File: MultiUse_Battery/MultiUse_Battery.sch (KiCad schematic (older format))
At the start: 14 parts, among them IC1 ATMEGA328P-AU, P1 CONN_01X02, P2 CONN_01X01, P3 CONN_01X03, P4 CONN_01X03, P5 CONN_02X03, P6 CONN_01X02, P7 CONN_01X02, U1 MAX1724, U3 RFM69HW

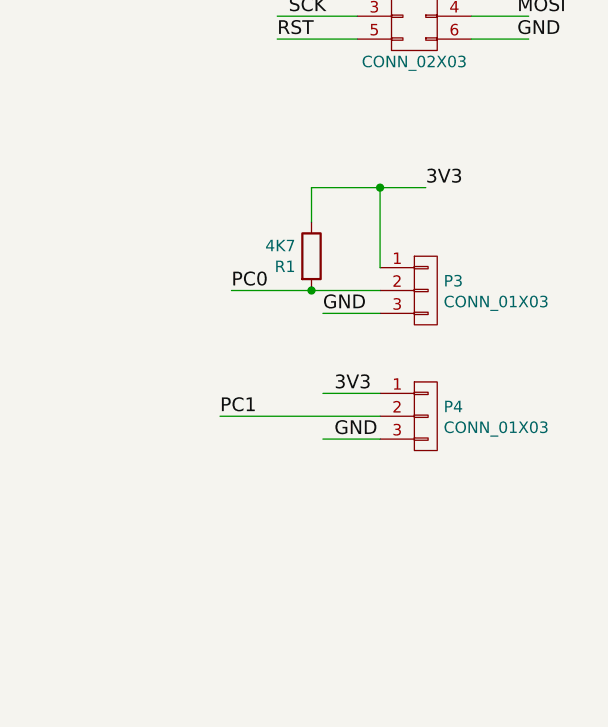
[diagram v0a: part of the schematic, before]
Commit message: Ajout README.md Modification orientation support pile CR2032 Ajout d'une PULLUP sur 2eme entrée
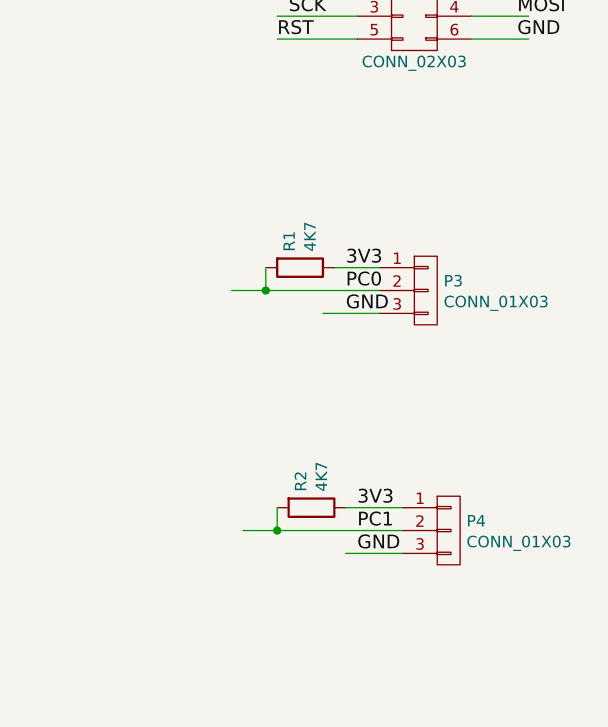
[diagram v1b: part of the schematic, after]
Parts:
- added R2: 4K7, Resistors_SMD:R_1206_HandSoldering, symbol R
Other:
- moved on the sheet: P4, R1
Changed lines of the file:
@@
 L CONN_01X03 P4
 U 1 1 587A3CDC
-P 9050 4400
-F 0 "P4" H 9128 4441 50  0000 L CNN
-F 1 "CONN_01X03" H 9128 4350 50  0000 L CNN
-F 2 "Pin_Headers:Pin_Header_Straight_1x03" H 9050 4400 50  0001 C CNN
-F 3 "" H 9050 4400 50  0000 C CNN
-	1    9050 4400
+P 9150 4900
+F 0 "P4" H 9228 4941 50  0000 L CNN
+F 1 "CONN_01X03" H 9228 4850 50  0000 L CNN
+F 2 "Pin_Headers:Pin_Header_Straight_1x03" H 9150 4900 50  0001 C CNN
+F 3 "" H 9150 4900 50  0000 C CNN
+	1    9150 4900
 	1    0    0    -1
 $EndComp
@@
 L R R1
 U 1 1 587A3DC5
-P 8550 3700
-F 0 "R1" H 8480 3654 50  0000 R CNN
-F 1 "4K7" H 8480 3745 50  0000 R CNN
-F 2 "Resistors_SMD:R_1206_HandSoldering" V 8480 3700 50  0001 C CNN
-F 3 "" H 8550 3700 50  0000 C CNN
-	1    8550 3700
-	1    0    0    -1
+P 8500 3750
+F 0 "R1" H 8430 3704 50  0000 R CNN
+F 1 "4K7" H 8430 3795 50  0000 R CNN
+F 2 "Resistors_SMD:R_1206_HandSoldering" V 8430 3750 50  0001 C CNN
+F 3 "" H 8500 3750 50  0000 C CNN
+	1    8500 3750
+	0    1    1    0
 $EndComp
 $Comp
@@
 Text Label 5900 5650 0    60   ~ 0
 3V3
-Text Label 9050 3400 0    60   ~ 0
-3V3
-Text Label 8600 3950 0    60   ~ 0
-GND
-Text Label 8650 4300 0    60   ~ 0
-3V3
-Text Label 8650 4500 0    60   ~ 0
+Text Label 8700 3750 0    60   ~ 0
+3V3
+Text Label 8700 3950 0    60   ~ 0
+GND
+Text Label 8750 4800 0    60   ~ 0
+3V3
+Text Label 8750 5000 0    60   ~ 0
 GND
 $Comp
@@
 Text Label 5000 3450 0    60   ~ 0
 PC1
-Text Label 8200 3850 0    60   ~ 0
+Text Label 8700 3850 0    60   ~ 0
 PC0
-Text Label 8150 4400 0    60   ~ 0
+Text Label 8750 4900 0    60   ~ 0
 PC1
 $Comp
@@
 	8200 3850 8850 3850
 Wire Wire Line
-	8850 3750 8850 3400
-Wire Wire Line
 	8850 3950 8600 3950
-Connection ~ 8550 3850
-Wire Wire Line
-	8550 3550 8550 3400
-Wire Wire Line
-	8550 3400 9050 3400
-Connection ~ 8850 3400
-Wire Wire Line
-	8850 4300 8600 4300
-Wire Wire Line
-	8850 4500 8600 4500
-Wire Wire Line
-	8850 4400 8150 4400
+Connection ~ 8350 3850
+Wire Wire Line
+	8950 4800 8700 4800
+Wire Wire Line
+	8950 5000 8700 5000
+Wire Wire Line
+	8950 4900 8250 4900
 Wire Wire Line
 	6200 6000 6350 6000
@@
 Text Label 1900 2200 0    60   ~ 0
 GND
+$Comp
+L R R2
+U 1 1 587CCD31
+P 8550 4800
+F 0 "R2" H 8480 4754 50  0000 R CNN
+F 1 "4K7" H 8480 4845 50  0000 R CNN
+F 2 "Resistors_SMD:R_1206_HandSoldering" V 8480 4800 50  0001 C CNN
+F 3 "" H 8550 4800 50  0000 C CNN
+	1    8550 4800
+	0    1    1    0
+$EndComp
+Wire Wire Line
+	8400 4800 8400 4900
+Connection ~ 8400 4900
+Wire Wire Line
+	8850 3750 8650 3750
+Wire Wire Line
+	8350 3750 8350 3850
 $EndSCHEMATC

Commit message: modifs
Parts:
- added U2: AP111733, TO_SOT_Packages_SMD:SOT-223, symbol AP111733
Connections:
- wire segments 60 -> 64
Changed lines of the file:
@@
 Wire Wire Line
 	8350 3750 8350 3850
+$Comp
+L AP111733 U2
+U 1 1 587CDB07
+P 6350 1000
+F 0 "U2" H 6450 750 50  0000 C CNN
+F 1 "AP111733" H 6350 1250 50  0000 C CNN
+F 2 "TO_SOT_Packages_SMD:SOT-223" H 6350 650 50  0001 C CNN
+F 3 "" H 6450 750 50  0000 C CNN
+	1    6350 1000
+	1    0    0    -1
+$EndComp
+Wire Wire Line
+	6650 1000 7100 1000
+Wire Wire Line
+	6350 1300 6350 1400
+Wire Wire Line
+	6350 1400 7100 1400
+Wire Wire Line
+	6050 1000 5650 1000
+Text Label 5700 1000 0    60   ~ 0
+VIN
+Text Label 6800 1400 0    60   ~ 0
+GND
+Text Label 6800 1000 0    60   ~ 0
+3V3
 $EndSCHEMATC
